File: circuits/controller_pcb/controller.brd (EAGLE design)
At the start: 38.8 x 16 mm, 50 parts, among them IC1 DS1820, J3 USB-MICROB", Q2 FDN340P, Q3 SI2333DS, Q5 BSS138, U1 ATMEGA328P_TQFP, U2 MIC5219 5V

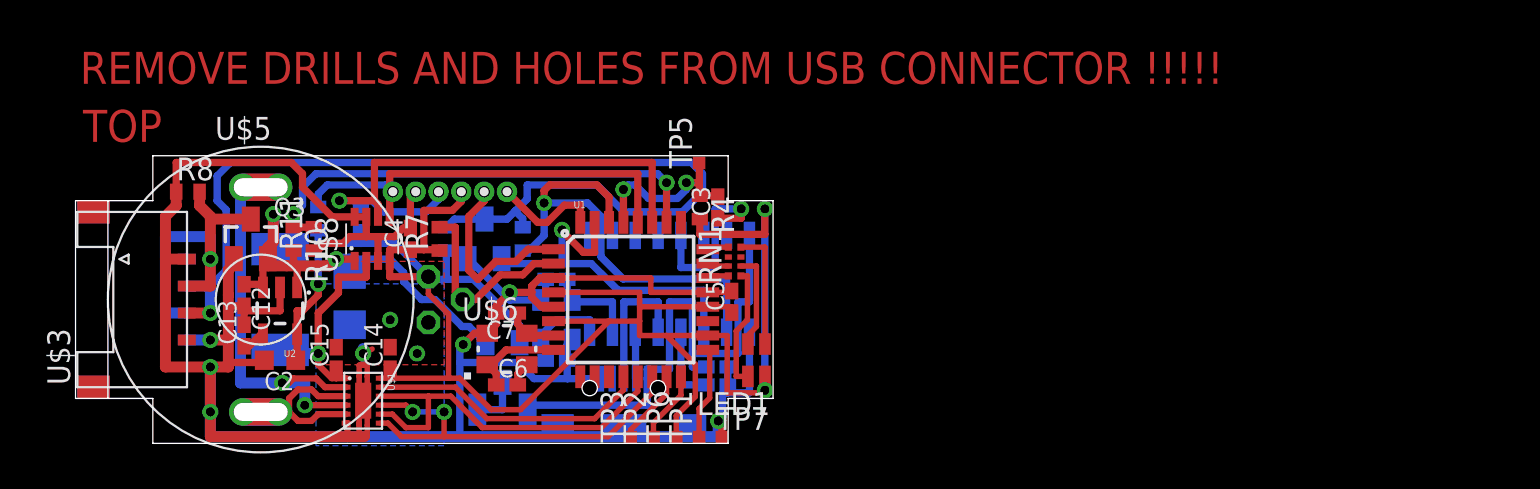
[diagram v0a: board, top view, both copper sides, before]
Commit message: Updated controller circuit - UNTESTED
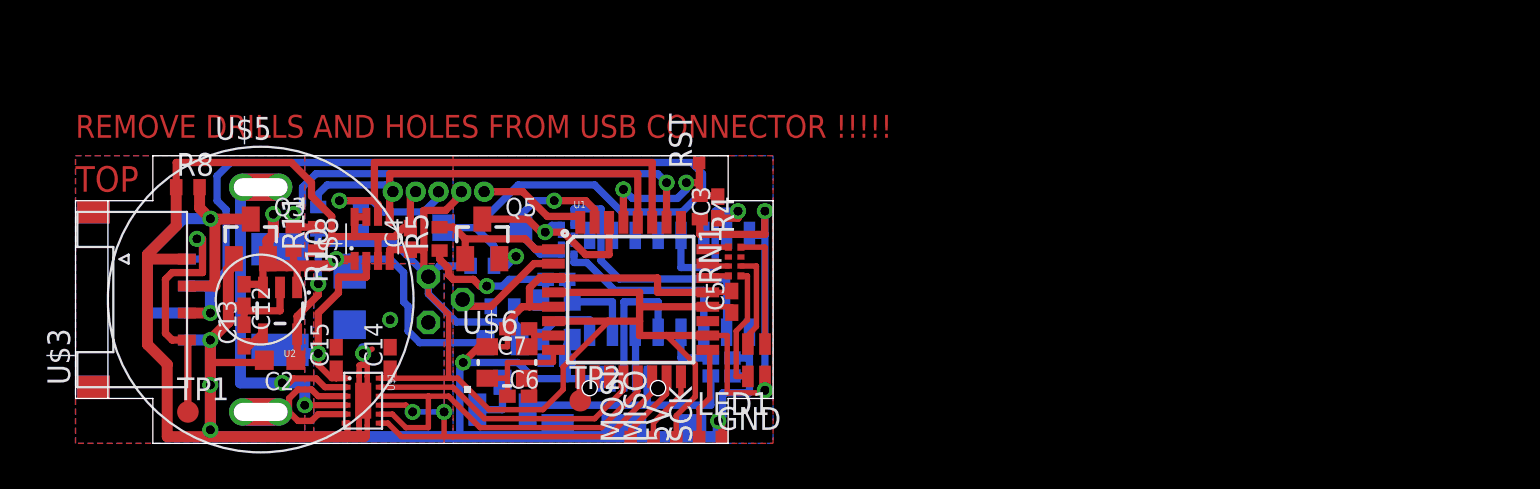
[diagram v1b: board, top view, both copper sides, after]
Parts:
- removed U$7: 1X6, headers(.05in):1X6
- added D1: IN5819, SparkFun-DiscreteSemi:SMA-DIODE
- added MISO, SCK: TPTP07SQ, testpad:TP07SQ
- added RN2: (no value), resistor-dil:YC124
- added U$10: 1X5, headers(.05in):1X5
- R5: value 1k -> 10k
- TP1, TP2: value TPTP07SQ -> PTR1TP12R; device testpad:TP07SQ -> testpad:TP12R
- moved TP1 28.5 mm to (6.25, 1.75), turned to 0 degrees
- moved R7 5.13 mm to (23.8, 7.62), flipped to the bottom, turned to 0 degrees
- moved R5 4.62 mm to (20.2, 11.4), flipped to the top
- moved TP2 4.55 mm to (28.1, 2.38), turned to 0 degrees
- moved R6 2.50 mm to (22.6, 9.88), turned to 180 degrees
- moved C8 1.52 mm to (35.9, 4.75)
- moved C7 1.08 mm to (24.6, 6.38)
- moved C6 0.88 mm to (24.6, 2.62)
- moved U$6 0.75 mm to (24.0, 4.50)
- moved C11 0.56 mm to (35.9, 3.75)
- moved R8 0.25 mm to (6.25, 14.2)
- moved Q5 0.12 mm to (22.6, 11.4), flipped to the top
- moved R11 0.12 mm to (13.4, 11.4)
- renumbered TP3 to MOSI, TP5 to RST, TP6 to 5V, TP7 to GND
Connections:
- removed net PWM: U$7.2, U1.1
- new net HD_DIR: Q5.1, R5.2, U1.1
- new net N$13: TP2.TP, U1.9
- new net N$15: RN2.8, U$2.3
- new net N$6: RN2.5, U$2.2
- new net N$7: TP1.TP, U$3.P$4, U$4.P$4
- net 5V: now also U$10.2, U$2.16; no longer U$7.3
- net DATA: now also D1.A, Q5.2; no longer Q5.3, R5.2
- net GND: now also R5.1, U$10.4; no longer Q5.2, U$7.5
- net INT: now also U$10.1; no longer U$7.1
- net N$10: no longer U$2.16
- net N$14: now also SCK.TP; no longer TP1.TP
- net N$4: now also MISO.TP; no longer TP2.TP
- net RX: now also Q5.3, RN2.4; no longer R5.1, U$2.2
- net SCL: now also U$10.5; no longer U$7.6
- net SDA: now also U$10.3; no longer U$7.4
- net TX: now also D1.C, RN2.1; no longer Q5.1, U$2.3
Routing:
- net N$6: track 0.00 -> 15.7 mm
- net N$10: track 29.3 -> 14.1 mm
- net N$7: track 0.00 -> 15.1 mm, vias 0 -> 1
- net RX: track 25.7 -> 10.7 mm
- net N$15: track 0.00 -> 10.7 mm
- net TX: track 20.4 -> 9.81 mm
- net PWM: track 10.3 -> 0.00 mm
- net GND: track 167.0 -> 176.1 mm, vias 9 -> 8
- net HD_DIR: track 0.00 -> 7.94 mm
- net DATA: track 57.3 -> 61.2 mm, vias 1 -> 2
- net 1WIRE: track 10.9 -> 7.92 mm
- net VIN: track 27.8 -> 29.3 mm
- net N$13: track 0.00 -> 1.33 mm
- net N$11: track 4.34 -> 3.09 mm
- net VCC: track 18.2 -> 19.3 mm
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
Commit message: Corrected Q5 orientation - UNTESTED
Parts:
- moved R6 4.98 mm to (18.1, 12.0)
- moved R7 0.38 mm to (23.8, 8.00)
- moved Q5 0.25 mm to (22.9, 11.4), turned to 90 degrees
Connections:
- net HD_DIR renamed DIR
- net DATA: now also Q5.3; no longer Q5.2
- net RX: now also Q5.2; no longer Q5.3
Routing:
- net 5V: track 110.1 -> 108.7 mm
- net RX: track 10.7 -> 9.56 mm
- net DIR: track 7.94 -> 8.94 mm
- net GND: track 176.1 -> 175.6 mm
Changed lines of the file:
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@@
 <setting verticaltext="up"/>
 </settings>
-<grid distance="0.5" unitdist="mm" unit="mm" style="lines" multiple="1" display="no" altdistance="0.025" altunitdist="inch" altunit="inch"/>
+<grid distance="1" unitdist="mm" unit="mm" style="lines" multiple="1" display="no" altdistance="0.025" altunitdist="inch" altunit="inch"/>
 <layers>
 <layer number="1" name="Top" color="4" fill="1" visible="yes" active="yes"/>
@@
 <element name="C7" library="rcl" package="C0402K" value="22p" x="24.625" y="6.375" rot="R180"/>
 <element name="R5" library="rcl" package="R0402" value="10k" x="20.25" y="11.375" rot="R90"/>
-<element name="R6" library="rcl" package="R0402" value="4k7" x="22.625" y="9.875" rot="MR180"/>
+<element name="R6" library="rcl" package="R0402" value="4k7" x="18.125" y="12" rot="MR180"/>
 <element name="Q2" library="transistor-fet" package="SSOT-3" value="FDN340P" x="23.75" y="4.5" rot="MR180"/>
 <element name="RN1" library="resistor-dil" package="YC124" value="" x="36.6625" y="10.115" rot="R270">
@@
 <element name="C10" library="rcl" package="C0402K" value="22p" x="26.75" y="9.125" rot="MR0"/>
 <element name="C11" library="rcl" package="C0402K" value="100n" x="35.9375" y="3.75" rot="MR180"/>
-<element name="R7" library="rcl" package="R0402" value="4k7" x="23.75" y="7.625" rot="MR0"/>
+<element name="R7" library="rcl" package="R0402" value="4k7" x="23.75" y="8" rot="MR0"/>
 <element name="U$8" library="INA219AIDCNR" package="SOT23-8L" value="INA219AIDCNR" x="16.5" y="11.375"/>
 <element name="Q3" library="transistor-fet" package="SOT23" value="SI2333DS" x="9.75" y="11.375"/>
@@
 <element name="C13" library="rcl" package="C0402K" value="100n" x="9.375" y="6" rot="R90"/>
 <element name="C14" library="rcl" package="C0402K" value="100n" x="17.5" y="4.75" rot="R90"/>
-<element name="Q5" library="transistor-fet" package="SOT23" value="BSS138" x="22.625" y="11.375"/>
+<element name="Q5" library="transistor-fet" package="SOT23" value="BSS138" x="22.875" y="11.375" rot="R90"/>
 <element name="R10" library="rcl" package="R0402" value="" x="12.125" y="11.375" rot="R270"/>
 <element name="R11" library="rcl" package="R0402" value="" x="13.375" y="11.375" rot="R90"/>
@@
 <wire x1="25.8" y1="9.2" x2="25.25" y2="8.65" width="0.4064" layer="1"/>
 <wire x1="25.25" y1="8.65" x2="25.25" y2="7.6" width="0.4064" layer="1"/>
-<via x="22.875" y="8.75" extent="1-16" drill="0.5" shape="octagon"/>
-<wire x1="20.25" y1="10.25" x2="20.75" y2="9.75" width="0.4064" layer="1"/>
+<via x="22.875" y="9.125" extent="1-16" drill="0.5" shape="octagon"/>
 <wire x1="20.25" y1="10.25" x2="20.25" y2="10.725" width="0.4064" layer="1"/>
-<wire x1="26.15" y1="9.125" x2="24.125" y2="9.125" width="0.4064" layer="16"/>
-<wire x1="24.125" y1="9.125" x2="23.75" y2="8.75" width="0.4064" layer="16"/>
-<wire x1="22.875" y1="8.75" x2="23.75" y2="8.75" width="0.4064" layer="16"/>
-<wire x1="22.125" y1="9.125" x2="22.5" y2="8.75" width="0.4064" layer="1"/>
-<wire x1="22.5" y1="8.75" x2="22.875" y2="8.75" width="0.4064" layer="1"/>
+<wire x1="26.15" y1="9.125" x2="22.875" y2="9.125" width="0.4064" layer="16"/>
 <wire x1="36.5375" y1="4.75" x2="37.485" y2="4.75" width="0.4064" layer="16"/>
 <wire x1="37.485" y1="4.75" x2="37.485" y2="3.75" width="0.4064" layer="16"/>
 <wire x1="36.5375" y1="3.75" x2="37.485" y2="3.75" width="0.4064" layer="16"/>
-<wire x1="20.75" y1="9.75" x2="20.75" y2="9.375" width="0.4064" layer="1"/>
-<wire x1="20.75" y1="9.375" x2="21" y2="9.125" width="0.4064" layer="1"/>
-<wire x1="21" y1="9.125" x2="22.125" y2="9.125" width="0.4064" layer="1"/>
+<wire x1="20.25" y1="10.25" x2="21.375" y2="9.125" width="0.4064" layer="1"/>
+<wire x1="21.375" y1="9.125" x2="22.875" y2="9.125" width="0.4064" layer="1"/>
 <wire x1="13.375" y1="10.725" x2="13.6" y2="10.725" width="0.4064" layer="1"/>
 <wire x1="13.6" y1="10.725" x2="14.25" y2="11.375" width="0.4064" layer="1"/>
@@
 <contactref element="5V" pad="TP"/>
 <via x="13.5" y="8.875" extent="1-16" drill="0.5" shape="octagon"/>
-<wire x1="17.77" y1="11.125" x2="15.875" y2="11.125" width="0.4064" layer="16"/>
+<wire x1="17.77" y1="11.125" x2="17.475" y2="11.125" width="0.4064" layer="16"/>
+<wire x1="17.475" y1="11.125" x2="15.875" y2="11.125" width="0.4064" layer="16"/>
 <wire x1="15.875" y1="11.125" x2="13.5" y2="11.125" width="0.4064" layer="16"/>
 <wire x1="13.5" y1="8.875" x2="13.5" y2="11.125" width="0.4064" layer="16"/>
@@
 <wire x1="21.1875" y1="6.75" x2="19.625" y2="8.3125" width="0.4064" layer="16"/>
 <wire x1="19.625" y1="8.3125" x2="19.625" y2="9.27" width="0.4064" layer="16"/>
-<wire x1="24.4" y1="7.625" x2="24.4" y2="6.775" width="0.4064" layer="16"/>
+<wire x1="24.4" y1="8" x2="24.4" y2="6.775" width="0.4064" layer="16"/>
+<wire x1="17.475" y1="12" x2="17.475" y2="11.125" width="0.4064" layer="16"/>
 <wire x1="24.4" y1="6.775" x2="24.375" y2="6.75" width="0.4064" layer="16"/>
-<wire x1="21.975" y1="9.875" x2="20.23" y2="9.875" width="0.4064" layer="16"/>
-<wire x1="20.23" y1="9.875" x2="19.625" y2="9.27" width="0.4064" layer="16"/>
 </signal>
 <signal name="INT">
@@
 <contactref element="U1" pad="30"/>
 <via x="26.125" y="11.75" extent="1-16" drill="0.5" shape="octagon"/>
-<contactref element="Q5" pad="3"/>
 <contactref element="RN2" pad="4"/>
 <wire x1="26.125" y1="11.75" x2="27.125" y2="11.75" width="0.4064" layer="1"/>
@@
 <wire x1="27.025" y1="12.13" x2="26.505" y2="12.13" width="0.4064" layer="16"/>
 <wire x1="26.505" y1="12.13" x2="26.125" y2="11.75" width="0.4064" layer="16"/>
-<wire x1="22.625" y1="12.475" x2="25.15" y2="12.475" width="0.4064" layer="1"/>
-<wire x1="25.15" y1="12.475" x2="25.875" y2="11.75" width="0.4064" layer="1"/>
 <wire x1="26.125" y1="11.75" x2="25.875" y2="11.75" width="0.4064" layer="1"/>
+<contactref element="Q5" pad="2"/>
+<wire x1="23.975" y1="12.325" x2="24.8" y2="12.325" width="0.4064" layer="1"/>
+<wire x1="24.8" y1="12.325" x2="25.375" y2="11.75" width="0.4064" layer="1"/>
+<wire x1="26.125" y1="11.75" x2="25.375" y2="11.75" width="0.4064" layer="1"/>
 </signal>
 <signal name="DATA">
@@
 <wire x1="34.875" y1="14" x2="33.75" y2="12.875" width="0.4064" layer="16"/>
 <contactref element="D1" pad="A"/>
-<contactref element="Q5" pad="2"/>
-<wire x1="28.875" y1="14.375" x2="24.625" y2="14.375" width="0.4064" layer="16"/>
-<via x="24.5" y="10.4" extent="1-16" drill="0.5" shape="octagon"/>
-<wire x1="24.625" y1="14.375" x2="22.25" y2="12" width="0.4064" layer="16"/>
+<wire x1="28.875" y1="14.375" x2="24.875" y2="14.375" width="0.4064" layer="16"/>
+<via x="21.75" y="10.025" extent="1-16" drill="0.5" shape="octagon"/>
+<wire x1="24.875" y1="14.375" x2="22.5" y2="12" width="0.4064" layer="16"/>
 <wire x1="20.75" y1="12" x2="20.475" y2="12" width="0.4064" layer="16"/>
-<wire x1="22.25" y1="12" x2="20.475" y2="12" width="0.4064" layer="16"/>
-<wire x1="23.275" y1="9.875" x2="23.975" y2="9.875" width="0.4064" layer="16"/>
-<wire x1="23.975" y1="9.875" x2="24.5" y2="10.4" width="0.4064" layer="16"/>
-<wire x1="22.25" y1="12" x2="23.275" y2="10.975" width="0.4064" layer="16"/>
-<wire x1="23.275" y1="10.975" x2="23.275" y2="9.875" width="0.4064" layer="16"/>
-<wire x1="24.5" y1="10.4" x2="23.7" y2="10.4" width="0.4064" layer="1"/>
-<wire x1="23.7" y1="10.4" x2="23.575" y2="10.275" width="0.4064" layer="1"/>
+<wire x1="22.5" y1="12" x2="20.475" y2="12" width="0.4064" layer="16"/>
+<contactref element="Q5" pad="3"/>
+<wire x1="21.75" y1="10.025" x2="21.75" y2="11.375" width="0.4064" layer="1"/>
+<wire x1="21.75" y1="11.375" x2="21.775" y2="11.375" width="0.4064" layer="1"/>
+<wire x1="18.775" y1="12" x2="20.475" y2="12" width="0.4064" layer="16"/>
+<wire x1="21.75" y1="10.025" x2="22.5" y2="10.775" width="0.4064" layer="16"/>
+<wire x1="22.5" y1="10.775" x2="22.5" y2="12" width="0.4064" layer="16"/>
 </signal>
 <signal name="TX">
@@
 <wire x1="23.125" y1="7.625" x2="21.905" y2="7.625" width="0.4064" layer="1"/>
 <wire x1="21.53" y1="8" x2="21.905" y2="7.625" width="0.4064" layer="1"/>
-<wire x1="23.1" y1="7.625" x2="21.905" y2="7.625" width="0.4064" layer="16"/>
-<wire x1="21.905" y1="7.625" x2="21.53" y2="8" width="0.4064" layer="16"/>
+<wire x1="23.1" y1="8" x2="21.53" y2="8" width="0.4064" layer="16"/>
 </signal>
 <signal name="N$10">
@@
 <wire x1="27.725" y1="10.0625" x2="27.725" y2="10.53" width="0.4064" layer="16"/>
 </signal>
-<signal name="HD_DIR">
-<contactref element="Q5" pad="1"/>
+<signal name="DIR">
 <contactref element="R5" pad="2"/>
 <contactref element="U1" pad="1"/>
-<wire x1="25" y1="11.375" x2="21.675" y2="11.375" width="0.4064" layer="1"/>
-<wire x1="21.025" y1="12.025" x2="20.25" y2="12.025" width="0.4064" layer="1"/>
-<wire x1="21.025" y1="12.025" x2="21.675" y2="11.375" width="0.4064" layer="1"/>
-<wire x1="21.675" y1="10.275" x2="21.675" y2="11.375" width="0.4064" layer="1"/>
-<wire x1="26.5824" y1="10.8" x2="25.575" y2="10.8" width="0.4064" layer="1"/>
-<wire x1="25" y1="11.375" x2="25.575" y2="10.8" width="0.4064" layer="1"/>
+<contactref element="Q5" pad="1"/>
+<wire x1="20.25" y1="12.025" x2="20.525" y2="12.025" width="0.4064" layer="1"/>
+<wire x1="20.525" y1="12.025" x2="21.125" y2="12.625" width="0.4064" layer="1"/>
+<wire x1="21.125" y1="12.625" x2="22.875" y2="12.625" width="0.4064" layer="1"/>
+<wire x1="22.875" y1="12.625" x2="22.875" y2="10.425" width="0.4064" layer="1"/>
+<wire x1="23.975" y1="10.425" x2="22.875" y2="10.425" width="0.4064" layer="1"/>
+<wire x1="26.5824" y1="10.8" x2="25.175" y2="10.8" width="0.4064" layer="1"/>
+<wire x1="25.175" y1="10.8" x2="24.8" y2="10.425" width="0.4064" layer="1"/>
+<wire x1="23.975" y1="10.425" x2="24.8" y2="10.425" width="0.4064" layer="1"/>
 </signal>
 <signal name="N$7">
